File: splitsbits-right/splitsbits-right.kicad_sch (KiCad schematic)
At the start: 25 parts, among them J1 RJ45, J2 USB_A, SW4 SW_Push_45deg, U1 Pico

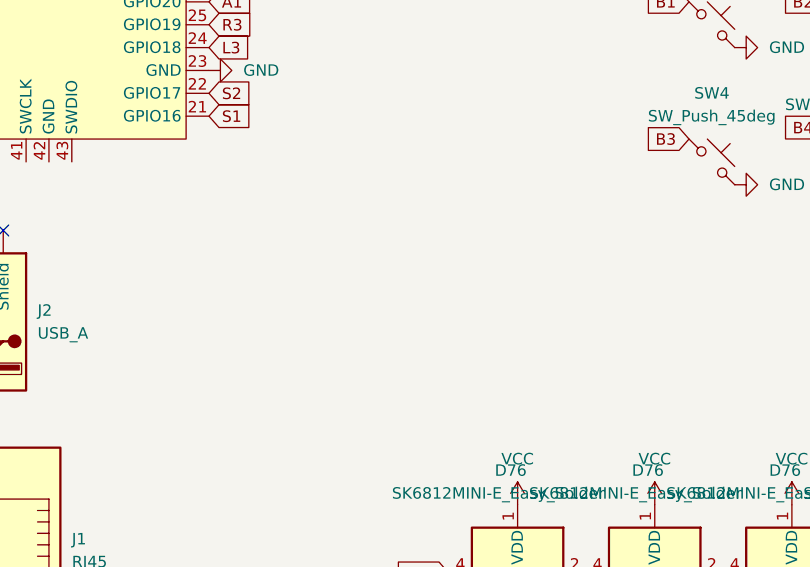
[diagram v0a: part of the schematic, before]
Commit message: Left Flatbox-Style Done
Pending Left WASD-Style
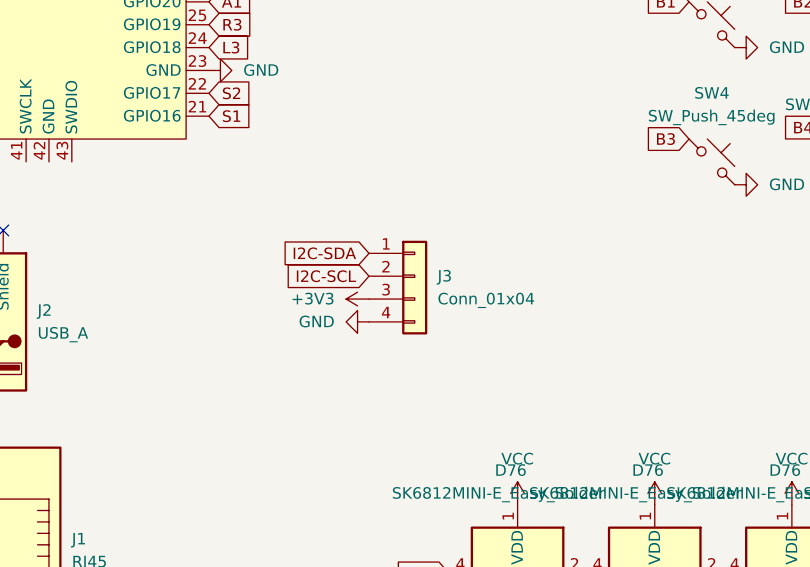
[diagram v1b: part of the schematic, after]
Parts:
- added J3: Conn_01x04, splitsbits:OLED_4Pin, symbol Connector_Generic:Conn_01x04
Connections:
- net +3V3: now also J3.3 (Pin_3)
- net GND: now also J3.4 (Pin_4)
- net I2C-SCL: now also J3.2 (Pin_2)
- net I2C-SDA: now also J3.1 (Pin_1)
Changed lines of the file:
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@@
+    )
+  )
+  (global_label "I2C-SDA" (shape input) (at 85.09 87.63 180) (fields_autoplaced)
+    (effects (font (size 1.27 1.27)) (justify right))
+    (property "Intersheetrefs" "${INTERSHEET_REFS}" (at 73.88 87.63 0)
+      (effects (font (size 1.27 1.27)) (justify right) hide)
     )
   )
@@
     )
   )
+  (global_label "I2C-SCL" (shape input) (at 85.09 90.17 180) (fields_autoplaced)
+    (effects (font (size 1.27 1.27)) (justify right))
+    (property "Intersheetrefs" "${INTERSHEET_REFS}" (at 73.9405 90.17 0)
+      (effects (font (size 1.27 1.27)) (justify right) hide)
+    )
+  )
   (global_label "R1" (shape input) (at 152.4 73.66 180) (fields_autoplaced)
     (effects (font (size 1.27 1.27)) (justify right))
@@
     )
   )
+  (symbol (lib_id "power:GND") (at 85.09 95.25 270) (unit 1)
+    (in_bom yes) (on_board yes) (dnp no) (fields_autoplaced)
+    (property "Reference" "#PWR011" (at 78.74 95.25 0)
+      (effects (font (size 1.27 1.27)) hide)
+    )
+    (property "Value" "GND" (at 81.28 95.25 90)
+      (effects (font (size 1.27 1.27)) (justify right))
+    )
+    (property "Footprint" "" (at 85.09 95.25 0)
+      (effects (font (size 1.27 1.27)) hide)
+    )
+    (property "Datasheet" "" (at 85.09 95.25 0)
+      (effects (font (size 1.27 1.27)) hide)
+    )
+    (pin "1")
+    (instances
+      (project "splitsbits-left"
+        (path "/7fb85417-7818-4ed5-af54-36dab7201c0b"
+          (reference "#PWR011") (unit 1)
+        )
+      )
+      (project "splitsbits-right"
+        (path "/bb99a10c-4e1e-47fc-8688-069dd31adefb"
+          (reference "#PWR040") (unit 1)
+        )
+      )
+    )
+  )
   (symbol (lib_id "power:GND") (at 140.97 78.74 90) (unit 1)
     (in_bom yes) (on_board yes) (dnp no) (fields_autoplaced)
@@
         (path "/bb99a10c-4e1e-47fc-8688-069dd31adefb"
           (reference "#PWR019") (unit 1)
+        )
+      )
+    )
+  )
+  (symbol (lib_id "Connector_Generic:Conn_01x04") (at 90.17 90.17 0) (unit 1)
+    (in_bom yes) (on_board yes) (dnp no) (fields_autoplaced)
+    (property "Reference" "J3" (at 92.71 90.17 0)
+      (effects (font (size 1.27 1.27)) (justify left))
+    )
+    (property "Value" "Conn_01x04" (at 92.71 92.71 0)
+      (effects (font (size 1.27 1.27)) (justify left))
+    )
+    (property "Footprint" "splitsbits:OLED_4Pin" (at 90.17 90.17 0)
+      (effects (font (size 1.27 1.27)) hide)
+    )
+    (property "Datasheet" "~" (at 90.17 90.17 0)
+      (effects (font (size 1.27 1.27)) hide)
+    )
+    (pin "1")
+    (pin "2")
+    (pin "3")
+    (pin "4")
+    (instances
+      (project "splitsbits-right"
+        (path "/bb99a10c-4e1e-47fc-8688-069dd31adefb"
+          (reference "J3") (unit 1)
         )
       )
@@
         )
       )
+    )
+  )
+  (symbol (lib_id "power:+3V3") (at 85.09 92.71 90) (unit 1)
+    (in_bom yes) (on_board yes) (dnp no) (fields_autoplaced)
+    (property "Reference" "#PWR016" (at 88.9 92.71 0)
+      (effects (font (size 1.27 1.27)) hide)
+    )
+    (property "Value" "+3V3" (at 81.28 92.71 90)
+      (effects (font (size 1.27 1.27)) (justify left))
+    )
+    (property "Footprint" "" (at 85.09 92.71 0)
+      (effects (font (size 1.27 1.27)) hide)
+    )
+    (property "Datasheet" "" (at 85.09 92.71 0)
+      (effects (font (size 1.27 1.27)) hide)
+    )
+    (pin "1")
+    (instances
+      (project "splitsbits-left"
+        (path "/7fb85417-7818-4ed5-af54-36dab7201c0b"
+          (reference "#PWR016") (unit 1)
+        )
+      )
+      (project "splitsbits-right"
+        (path "/bb99a10c-4e1e-47fc-8688-069dd31adefb"
+          (reference "#PWR041") (unit 1)
+        )
+      )
